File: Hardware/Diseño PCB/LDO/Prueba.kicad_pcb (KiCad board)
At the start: 2 copper layers, 98.5 x 100.5 mm, 58 parts, among them Q1 2N3904, Q10 BC557, Q11 BC547, Q12 BC557, Q13 BC557, Q14 BC547, Q15 BC557, Q16 BC547, Q17 BC557, Q18 BC547, Q19 BC547, Q2 BC547, Q3 BC547, Q4 BC557, Q5 BC557, Q6 BC547, Q7 BC547, Q8 IRF4905, Q9 BC547, U1 TL431LP, U4 LM324

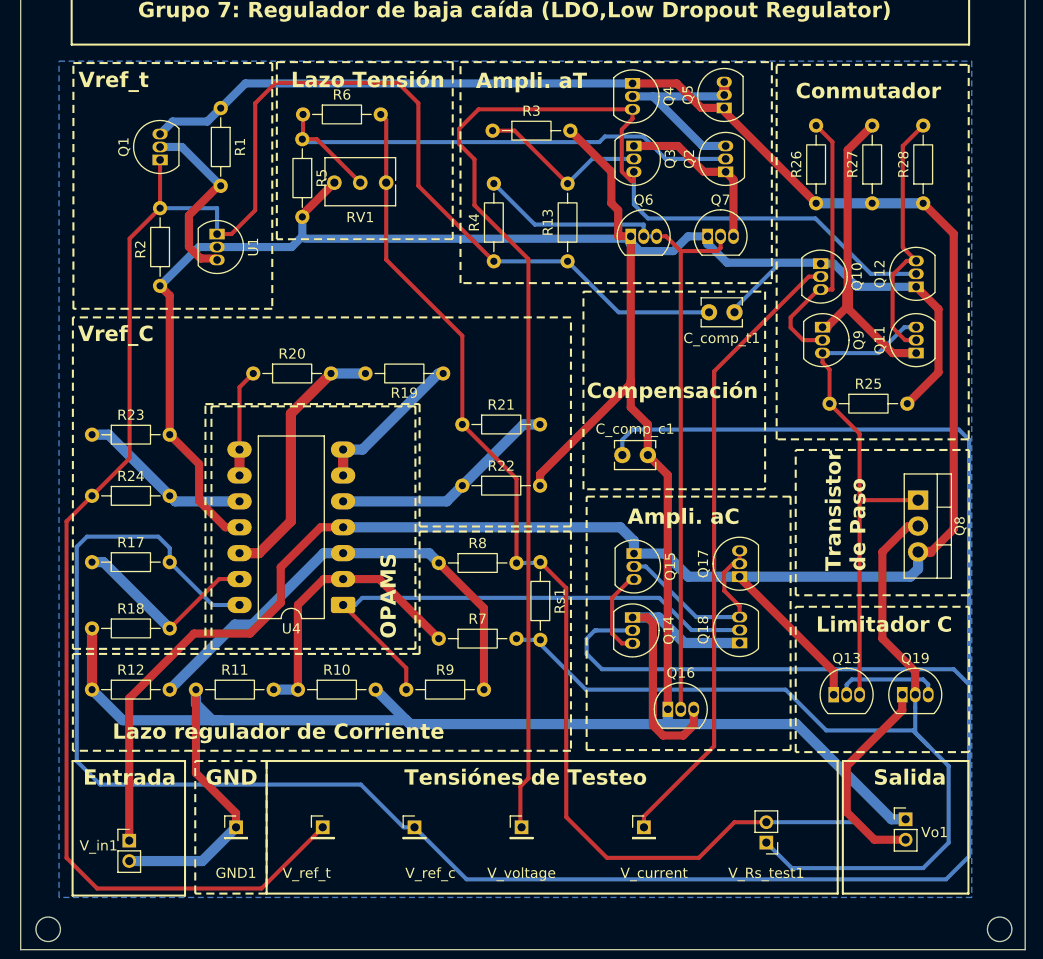
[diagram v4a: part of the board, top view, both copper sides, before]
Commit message: Diseño de PCB: Agregue preset lazo de corrente y compensacion de atraso de fase
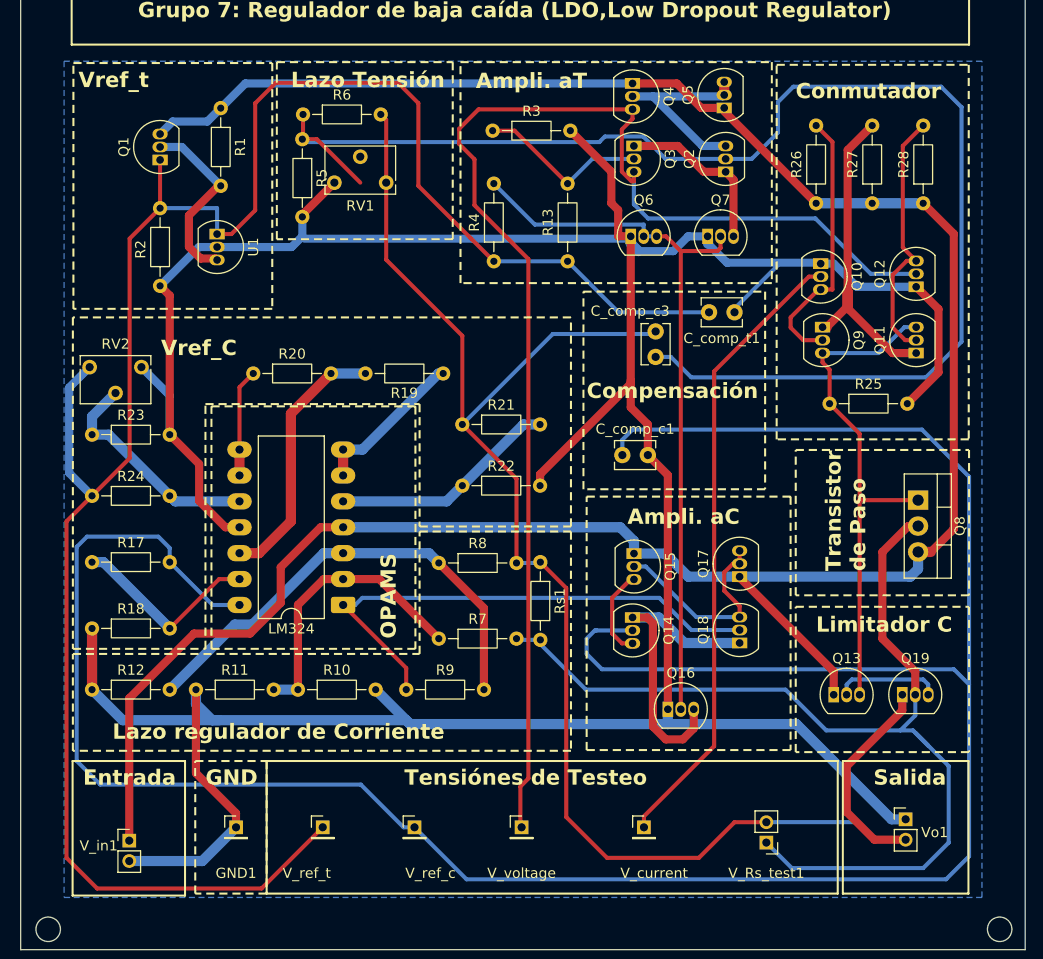
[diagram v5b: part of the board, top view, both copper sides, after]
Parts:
- added C_comp_c3: 2,2nF, Capacitor_THT:C_Disc_D3.8mm_W2.6mm_P2.50mm, F.Cu at (116.5, 179.5)
- added RV2: Preset, Potentiometer_THT:Potentiometer_Bourns_3266W_Vertical, F.Cu at (66.1, 180.5)
- RV1: footprint Potentiometer_THT:Potentiometer_Bourns_3266Y_Vertical -> Potentiometer_THT:Potentiometer_Bourns_3266W_Vertical
- renumbered U4 to LM324
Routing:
- net VF_fv: track 52.7 -> 136.6 mm
- net -V_Rs: track 136.2 -> 159.0 mm
- net Vref: track 183.8 -> 198.2 mm
- net GND: track 339.2 -> 347.0 mm
- net Net-(U4C-+): track 17.2 -> 22.2 mm
- net Vref_c: track 256.4 -> 254.3 mm
- net Net-(Q14-E): track 30.2 -> 30.8 mm

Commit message: Informe
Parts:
- renumbered LM324 to U4
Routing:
- removed copper zone on B.Cu, net GND
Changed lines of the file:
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@@
 		(descr "14-lead though-hole mounted DIP package, row spacing 10.16mm (400 mils), LongPads")
 		(tags "THT DIP DIL PDIP 2.54mm 10.16mm 400mil LongPads")
-		(property "Reference" "LM324"
+		(property "Reference" "U4"
 			(at 5.08 -2.33 0)
 			(layer "F.SilkS")
@@
 		(net "Net-(Q2-C)")
 	)
-	(zone
-		(net "GND")
-		(layer "B.Cu")
-		(hatch edge 0.5)
-		(connect_pads
-			(clearance 0.5)
-		)
-		(min_thickness 0.25)
-		(fill yes
-			(thermal_gap 0.5)
-			(thermal_bridge_width 0.5)
-			(island_removal_mode 0)
-		)
-		(polygon
-			(pts
-				(xy 58.5 232.5) (xy 148.5 232.5) (xy 148.5 150.5) (xy 58.5 150.5)
-			)
-		)
-	)
 	(embedded_fonts no)

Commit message: Informe y borneras
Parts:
- V_in1, Vo1: footprint Connector_PinHeader_2.00mm:PinHeader_1x02_P2.00mm_Vertical -> TerminalBlock:TerminalBlock_MaiXu_MX126-5.0-02P_1x02_P5.00mm
- moved Vo1 1.67 mm to (141.5, 223.2), turned to -90 degrees
- moved V_in1 1.08 mm to (65.0, 228.0), turned to 90 degrees
- renumbered V_Rs_test1 to V_Rs
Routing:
- net Vcc: track 239.6 -> 245.5 mm
- net VF_fv: track 136.6 -> 130.7 mm
- net GND: track 347.0 -> 349.7 mm
- net -V_Rs: track 159.0 -> 161.6 mm
- net Net-(Q14-E): track 30.8 -> 33.4 mm
- net +V_Rs: track 102.9 -> 101.0 mm
- net Vref_c: track 254.3 -> 256.2 mm
- net Net-(U4A-+): track 46.6 -> 47.6 mm
- net V_voltage: track 132.2 -> 131.7 mm
- added copper zone on B.Cu, net GND
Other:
- board size 98.5 x 100.5 mm -> 100 x 100 mm
- board text added: "Tensiones de Testeo"
- board text removed: "Tensiónes de Testeo"

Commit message: Diseño de PCB : Logo FIUBA + pistas
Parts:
- added G***: LOGO, LOGO, B.Cu at (73.7, 144.7)
- moved Rs1 1.30 mm to (106.5, 199.6)
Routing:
- net Vcc: track 245.5 -> 248.1 mm
- net V_voltage: track 131.7 -> 133.9 mm
- net Net-(Q11-C): track 32.2 -> 30.5 mm
- net GND: track 349.7 -> 351.2 mm
- net Vctrl: track 51.0 -> 52.4 mm
- net -V_Rs: track 161.6 -> 162.4 mm
- net +V_Rs: track 101.0 -> 101.8 mm
- net Net-(Q11-B): track 25.5 -> 26.1 mm
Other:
- outline, holes or cut-outs redrawn
